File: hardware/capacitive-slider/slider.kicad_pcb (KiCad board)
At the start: 2 copper layers, 128 x 18 mm, 6 parts, among them J1 CONN, U1 AT42QT2120

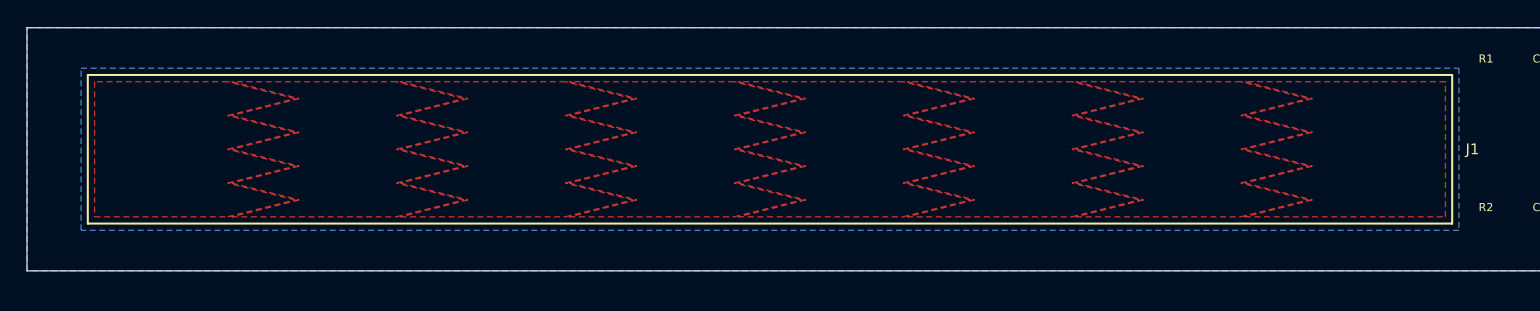
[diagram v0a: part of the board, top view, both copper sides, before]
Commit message: Fix KiCad 8 compatibility: update version and keepout zone syntax
- Bump format version from 20221018 (KiCad 7) to 20240108 (KiCad 8)
- Replace old (zone ... (attr (is_rule_area))) with (rule_area ...) syntax
  for the slider keepout zone, matching KiCad 8's expected format

https://claude.ai/code/session_01ExJ7gFQfT848CsR2EsnjBp
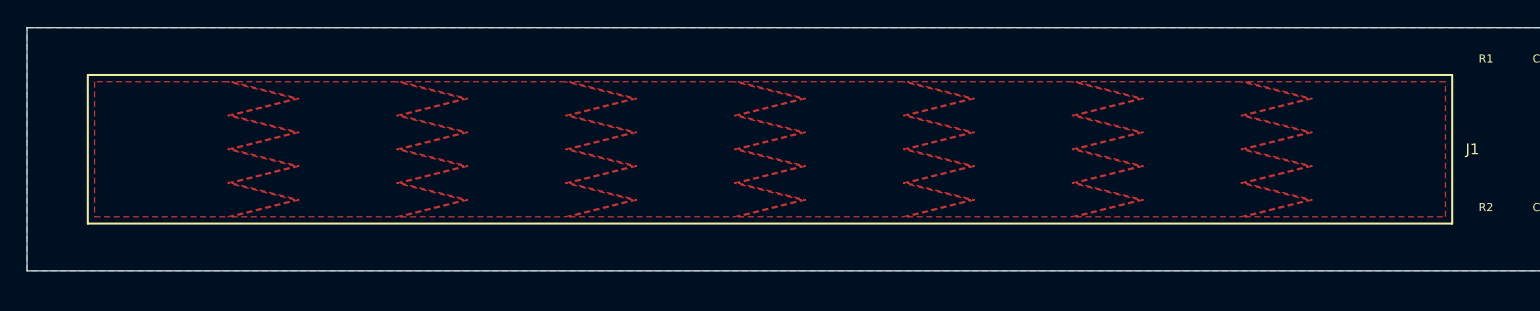
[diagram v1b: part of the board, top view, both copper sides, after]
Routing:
- removed copper zone on B.Cu, net (none)
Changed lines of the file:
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@@
-(kicad_pcb (version 20221018) (generator "arp3_slider_gen")
+(kicad_pcb (version 20240108) (generator "arp3_slider_gen")
   (general
     (thickness 1.6)
@@
     ))
   )
-  (zone (net 0) (net_name "") (layers "B.Cu")
-    (hatch edge 0.5)
-    (name "slider_keepout")
-    (attr (is_rule_area) (is_keepout_copper_pour) (is_keepout_via) (is_keepout_track))
+  (rule_area "slider_keepout" (id 00000000-0000-0000-0000-000000000010) (hatch edge 0.5) (connect_pads (clearance 0)) (min_thickness 0.25) (keepout (tracks not_allowed) (vias not_allowed) (pads allowed) (copperpour not_allowed) (footprints allowed))
+    (layer "B.Cu")
     (polygon (pts
       (xy 4 3) (xy 106 3)
